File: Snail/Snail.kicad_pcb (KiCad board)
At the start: 2 copper layers, 16 parts, among them J1 Arduino Nano SuperMini, SW0 SW_Push, SW1 SW_Push, SW2 SW_Push, SW3 SW_Push

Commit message: Lay out LED matrix
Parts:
- added C1: 10u, Capacitor_SMD:C_0603_1608Metric, F.Cu at (48.6, 79.7)
- added C105: 100n, Capacitor_SMD:C_0402_1005Metric, F.Cu at (76.0, 60.0)
- added C106: 100n, Capacitor_SMD:C_0402_1005Metric, F.Cu at (63.5, 60.0)
- added C107: 100n, Capacitor_SMD:C_0402_1005Metric, F.Cu at (51.0, 60.0)
- added C108: 100n, Capacitor_SMD:C_0402_1005Metric, F.Cu at (38.5, 60.0)
- added C109: 100n, Capacitor_SMD:C_0402_1005Metric, F.Cu at (26.0, 60.0)
- added C110: 100n, Capacitor_SMD:C_0402_1005Metric, F.Cu at (34.0, 53.0)
- added C111: 100n, Capacitor_SMD:C_0402_1005Metric, F.Cu at (46.5, 53.0)
- added C112: 100n, Capacitor_SMD:C_0402_1005Metric, F.Cu at (59.0, 53.0)
- added C113: 100n, Capacitor_SMD:C_0402_1005Metric, F.Cu at (71.5, 53.0)
- added C114: 100n, Capacitor_SMD:C_0402_1005Metric, F.Cu at (84.0, 53.0)
- added C115: 100n, Capacitor_SMD:C_0402_1005Metric, F.Cu at (76.0, 42.0)
- added C116: 100n, Capacitor_SMD:C_0402_1005Metric, F.Cu at (63.5, 42.0)
- added C117: 100n, Capacitor_SMD:C_0402_1005Metric, F.Cu at (51.0, 42.0)
- added C118: 100n, Capacitor_SMD:C_0402_1005Metric, F.Cu at (38.5, 42.0)
- added C119: 100n, Capacitor_SMD:C_0402_1005Metric, F.Cu at (26.0, 42.0)
- added C120: 100n, Capacitor_SMD:C_0402_1005Metric, F.Cu at (34.0, 35.0)
- added C121: 100n, Capacitor_SMD:C_0402_1005Metric, F.Cu at (46.5, 35.0)
- added C122: 100n, Capacitor_SMD:C_0402_1005Metric, F.Cu at (59.0, 35.0)
- added C123: 100n, Capacitor_SMD:C_0402_1005Metric, F.Cu at (71.5, 35.0)
- added C124: 100n, Capacitor_SMD:C_0402_1005Metric, F.Cu at (84.0, 35.0)
- added C125: 100n, Capacitor_SMD:C_0402_1005Metric, F.Cu at (76.0, 24.0)
- added C126: 100n, Capacitor_SMD:C_0402_1005Metric, F.Cu at (63.5, 24.0)
- added C127: 100n, Capacitor_SMD:C_0402_1005Metric, F.Cu at (51.0, 24.0)
- added C128: 100n, Capacitor_SMD:C_0402_1005Metric, F.Cu at (38.5, 24.0)
- added C129: 100n, Capacitor_SMD:C_0402_1005Metric, F.Cu at (26.0, 24.0)
- added C130: 100n, Capacitor_SMD:C_0402_1005Metric, F.Cu at (34.0, 17.0)
- added C131: 100n, Capacitor_SMD:C_0402_1005Metric, F.Cu at (46.5, 17.0)
- added C132: 100n, Capacitor_SMD:C_0402_1005Metric, F.Cu at (59.0, 17.0)
- added C133: 100n, Capacitor_SMD:C_0402_1005Metric, F.Cu at (71.5, 17.0)
- added C134: 100n, Capacitor_SMD:C_0402_1005Metric, F.Cu at (84.0, 17.0)
- added C2: 10u, Capacitor_SMD:C_0603_1608Metric, F.Cu at (51.1, 79.7)
- added D1: 1N5819, Diode_SMD:D_SOD-323, F.Cu at (55.9, 84.8)
- added D105: WS2812B, Local:LED_ARGB_5050, F.Cu at (80.0, 61.0)
- added D106: WS2812B, Local:LED_ARGB_5050, F.Cu at (67.5, 61.0)
- added D107: WS2812B, Local:LED_ARGB_5050, F.Cu at (55.0, 61.0)
- added D108: WS2812B, Local:LED_ARGB_5050, F.Cu at (42.5, 61.0)
- added D109: WS2812B, Local:LED_ARGB_5050, F.Cu at (30.0, 61.0)
- added D110: WS2812B, Local:LED_ARGB_5050, F.Cu at (30.0, 52.0)
- added D111: WS2812B, Local:LED_ARGB_5050, F.Cu at (42.5, 52.0)
- added D112: WS2812B, Local:LED_ARGB_5050, F.Cu at (55.0, 52.0)
- added D113: WS2812B, Local:LED_ARGB_5050, F.Cu at (67.5, 52.0)
- added D114: WS2812B, Local:LED_ARGB_5050, F.Cu at (80.0, 52.0)
- added D115: WS2812B, Local:LED_ARGB_5050, F.Cu at (80.0, 43.0)
- added D116: WS2812B, Local:LED_ARGB_5050, F.Cu at (67.5, 43.0)
- added D117: WS2812B, Local:LED_ARGB_5050, F.Cu at (55.0, 43.0)
- added D118: WS2812B, Local:LED_ARGB_5050, F.Cu at (42.5, 43.0)
- added D119: WS2812B, Local:LED_ARGB_5050, F.Cu at (30.0, 43.0)
- added D120: WS2812B, Local:LED_ARGB_5050, F.Cu at (30.0, 34.0)
- added D121: WS2812B, Local:LED_ARGB_5050, F.Cu at (42.5, 34.0)
- added D122: WS2812B, Local:LED_ARGB_5050, F.Cu at (55.0, 34.0)
- added D123: WS2812B, Local:LED_ARGB_5050, F.Cu at (67.5, 34.0)
- added D124: WS2812B, Local:LED_ARGB_5050, F.Cu at (80.0, 34.0)
- added D125: WS2812B, Local:LED_ARGB_5050, F.Cu at (80.0, 25.0)
- added D126: WS2812B, Local:LED_ARGB_5050, F.Cu at (67.5, 25.0)
- added D127: WS2812B, Local:LED_ARGB_5050, F.Cu at (55.0, 25.0)
- added D128: WS2812B, Local:LED_ARGB_5050, F.Cu at (42.5, 25.0)
- added D129: WS2812B, Local:LED_ARGB_5050, F.Cu at (30.0, 25.0)
- added D130: WS2812B, Local:LED_ARGB_5050, F.Cu at (30.0, 16.0)
- added D131: WS2812B, Local:LED_ARGB_5050, F.Cu at (42.5, 16.0)
- added D132: WS2812B, Local:LED_ARGB_5050, F.Cu at (55.0, 16.0)
- added D133: WS2812B, Local:LED_ARGB_5050, F.Cu at (67.5, 16.0)
- added D134: WS2812B, Local:LED_ARGB_5050, F.Cu at (80.0, 16.0)
- added Q1: MMBT3904, Package_TO_SOT_SMD:SOT-23, F.Cu at (51.7, 84.3)
- added R1: 4.7k, Resistor_SMD:R_0402_1005Metric, F.Cu at (48.5, 83.3)
- added R2: 10, Resistor_SMD:R_0402_1005Metric, F.Cu at (55.9, 83.2)
- moved BZ1 7.13 mm to (58.2, 95.0), turned to 180 degrees
- moved SW0 4.74 mm to (75.6, 81.2)
- moved SW3 4.74 mm to (66.6, 89.5)
- moved J1 4.74 mm to (35.1, 89.7)
- moved SW1 4.74 mm to (84.0, 89.2)
- moved SW2 4.74 mm to (75.7, 97.9)
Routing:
- net +5V: track 11.6 -> 81.5 mm, vias 6 -> 42
- net Net-(D130-DOUT): track 0.00 -> 17.9 mm
- net Net-(D120-DOUT): track 0.00 -> 17.9 mm
- net Net-(D110-DOUT): track 0.00 -> 17.9 mm
- net Net-(D125-DOUT): track 0.00 -> 17.9 mm
- net Net-(D115-DOUT): track 0.00 -> 17.9 mm
- net Net-(D105-DOUT): track 0.00 -> 17.9 mm
- net Net-(D132-DOUT): track 0.00 -> 8.97 mm
- net Net-(D131-DOUT): track 0.00 -> 8.97 mm
- net Net-(D128-DOUT): track 0.00 -> 8.97 mm
- net Net-(D127-DOUT): track 0.00 -> 8.97 mm
- net Net-(D126-DOUT): track 0.00 -> 8.97 mm
- net Net-(D122-DOUT): track 0.00 -> 8.97 mm
- net Net-(D121-DOUT): track 0.00 -> 8.97 mm
- net Net-(D118-DOUT): track 0.00 -> 8.97 mm
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
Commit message: 🚧 All components layout
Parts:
- added C135: 100n, Capacitor_SMD:C_0402_1005Metric, F.Cu at (120.2, 36.4)
- added C136: 100n, Capacitor_SMD:C_0402_1005Metric, F.Cu at (112.7, 36.4)
- added C137: 100n, Capacitor_SMD:C_0402_1005Metric, F.Cu at (105.2, 36.4)
- added D135: WS2812B, Local:LED_ARGB_3528, F.Cu at (121.0, 38.5)
- added D136: WS2812B, Local:LED_ARGB_3528, F.Cu at (113.5, 38.5)
- added D137: WS2812B, Local:LED_ARGB_3528, F.Cu at (106.0, 38.5)
- moved BZ1 50.6 mm to (98.2, 126.0)
- moved SW1 50.5 mm to (124.0, 120.0)
- moved SW2 50.1 mm to (115.0, 129.0)
- moved D1 50.0 mm to (95.9, 114.8)
- moved R2 50.0 mm to (95.9, 113.2)
- moved C1 50.0 mm to (88.6, 109.7)
- moved C100 50.0 mm to (74.0, 101.0)
- moved C101 50.0 mm to (86.5, 101.0)
- moved C102 50.0 mm to (99.0, 101.0)
- moved C103 50.0 mm to (111.5, 101.0)
- moved C104 50.0 mm to (124.0, 101.0)
- moved C105 50.0 mm to (116.0, 90.0)
- moved C106 50.0 mm to (103.5, 90.0)
- moved C107 50.0 mm to (91.0, 90.0)
- moved C108 50.0 mm to (78.5, 90.0)
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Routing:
- net +5V: track 81.5 -> 102.3 mm
- net /LIGHT_SD: track 0.00 -> 16.9 mm
- net Net-(BZ1--): track 0.00 -> 14.9 mm
- net Net-(BZ1-+): track 0.00 -> 13.6 mm
- net Net-(D134-DOUT): track 0.00 -> 7.80 mm
- net Net-(D136-DOUT): track 0.00 -> 4.56 mm
- net Net-(D135-DOUT): track 0.00 -> 4.56 mm
- net GND: track 0.00 -> 1.86 mm, vias 77 -> 81
- net Net-(Q1-B): track 0.00 -> 1.77 mm

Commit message: Finish layout & routing
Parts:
- moved SW2 2.60 mm to (114.0, 126.6)
- moved SW1 2.44 mm to (122.0, 118.6)
- moved BZ1 1.40 mm to (98.2, 124.6)
- moved C1 1.40 mm to (88.6, 108.3)
- moved C2 1.40 mm to (91.1, 108.3)
- moved J1 1.40 mm to (75.0, 118.3)
- moved R2 1.40 mm to (95.9, 111.8)
- moved SW3 1.40 mm to (106.0, 118.6)
- moved D1 1.40 mm to (95.9, 113.4)
- moved Q1 1.40 mm to (91.7, 112.9)
- moved R1 1.40 mm to (88.5, 111.9)
- moved C130 1.10 mm to (74.0, 48.1)
- moved C131 1.10 mm to (86.5, 48.1)
- moved C132 1.10 mm to (99.0, 48.1)
- moved C133 1.10 mm to (111.5, 48.1)
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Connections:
- J1 pad 10: unconnected-(J1-Pin_10-Pad10) -> /KEY_0
- J1 pad 11: unconnected-(J1-Pin_11-Pad11) -> /KEY_3
- J1 pad 12: /KEY_0 -> unconnected-(J1-Pin_12-Pad12)
- J1 pad 13: /KEY_1 -> unconnected-(J1-Pin_13-Pad13)
- J1 pad 14: /KEY_2 -> unconnected-(J1-Pin_14-Pad14)
- J1 pad 15: /KEY_3 -> /BUZZER
- J1 pad 6: /BUZZER -> unconnected-(J1-Pin_6-Pad6)
- J1 pad 8: unconnected-(J1-Pin_8-Pad8) -> /KEY_1
- J1 pad 9: unconnected-(J1-Pin_9-Pad9) -> /KEY_2
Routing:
- net +5V: track 102.3 -> 490.7 mm, vias 42 -> 0
- net /KEY_1: track 0.00 -> 69.3 mm
- net /KEY_2: track 0.00 -> 45.8 mm
- net /KEY_0: track 0.00 -> 41.5 mm
- net /KEY_3: track 0.00 -> 26.3 mm
- net Net-(D129-DOUT): track 0.00 -> 11.4 mm
- net Net-(D119-DOUT): track 0.00 -> 11.4 mm
- net Net-(D109-DOUT): track 0.00 -> 11.4 mm
- net Net-(D114-DOUT): track 0.00 -> 9.62 mm
- net Net-(D104-DOUT): track 0.00 -> 9.62 mm
- net Net-(D124-DOUT): track 0.00 -> 9.62 mm
- net Net-(D115-DOUT): track 17.9 -> 8.97 mm
- net Net-(D110-DOUT): track 17.9 -> 8.97 mm
- net Net-(D105-DOUT): track 17.9 -> 8.97 mm
- net Net-(D100-DOUT): track 17.9 -> 8.97 mm
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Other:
- board outline added: 64 x 98 mm

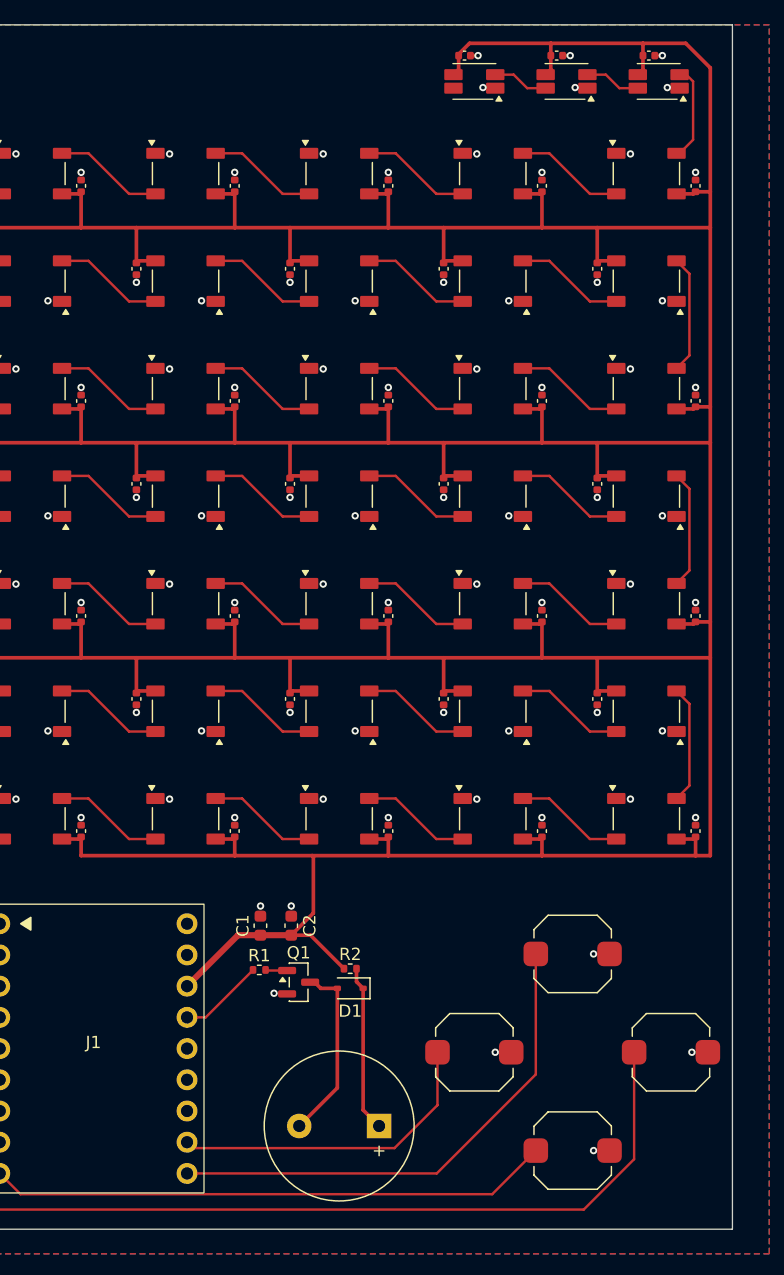
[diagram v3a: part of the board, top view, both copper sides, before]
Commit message: Revise board design for rounded tracks & teardrops
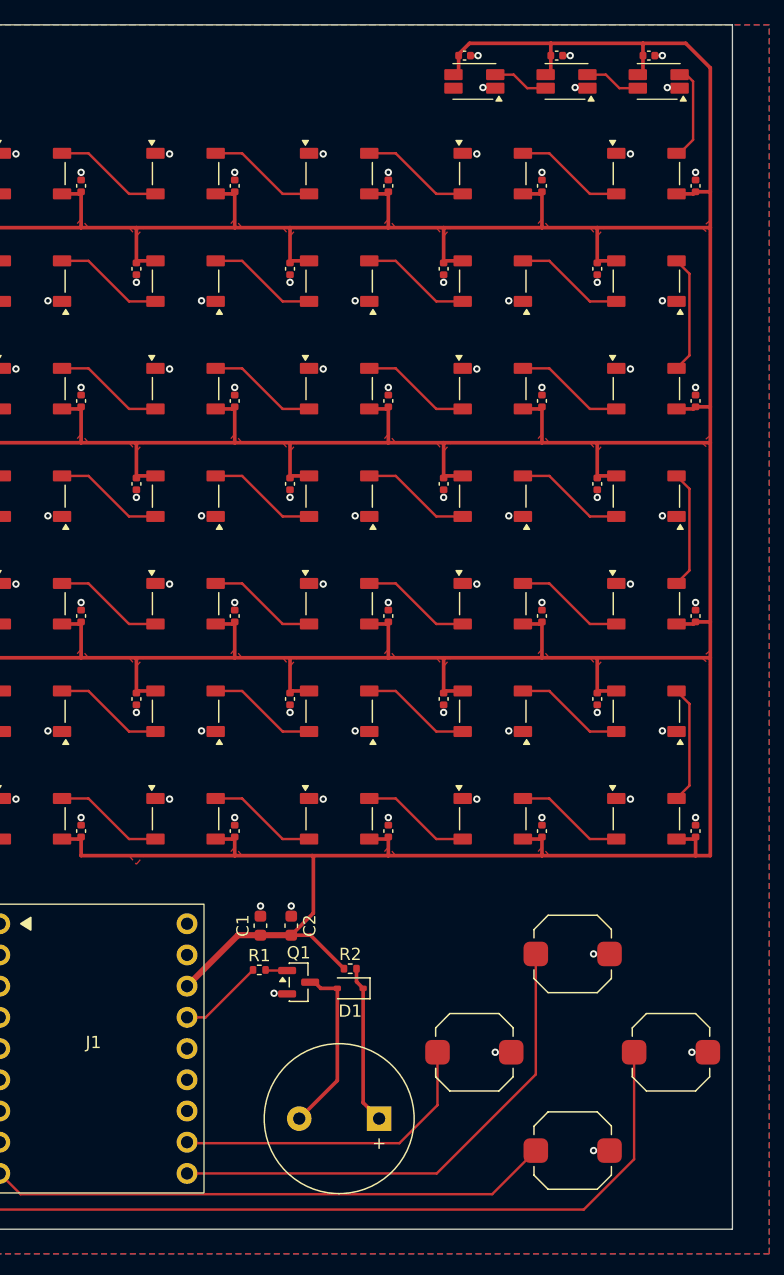
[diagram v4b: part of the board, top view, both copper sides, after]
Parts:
- moved BZ1 0.60 mm to (98.2, 124.0)
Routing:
- net +5V: track 490.7 -> 491.5 mm
- net Net-(BZ1--): track 14.9 -> 14.3 mm
- net Net-(BZ1-+): track 13.6 -> 13.0 mm
- added copper zone on F.Cu, net +5V

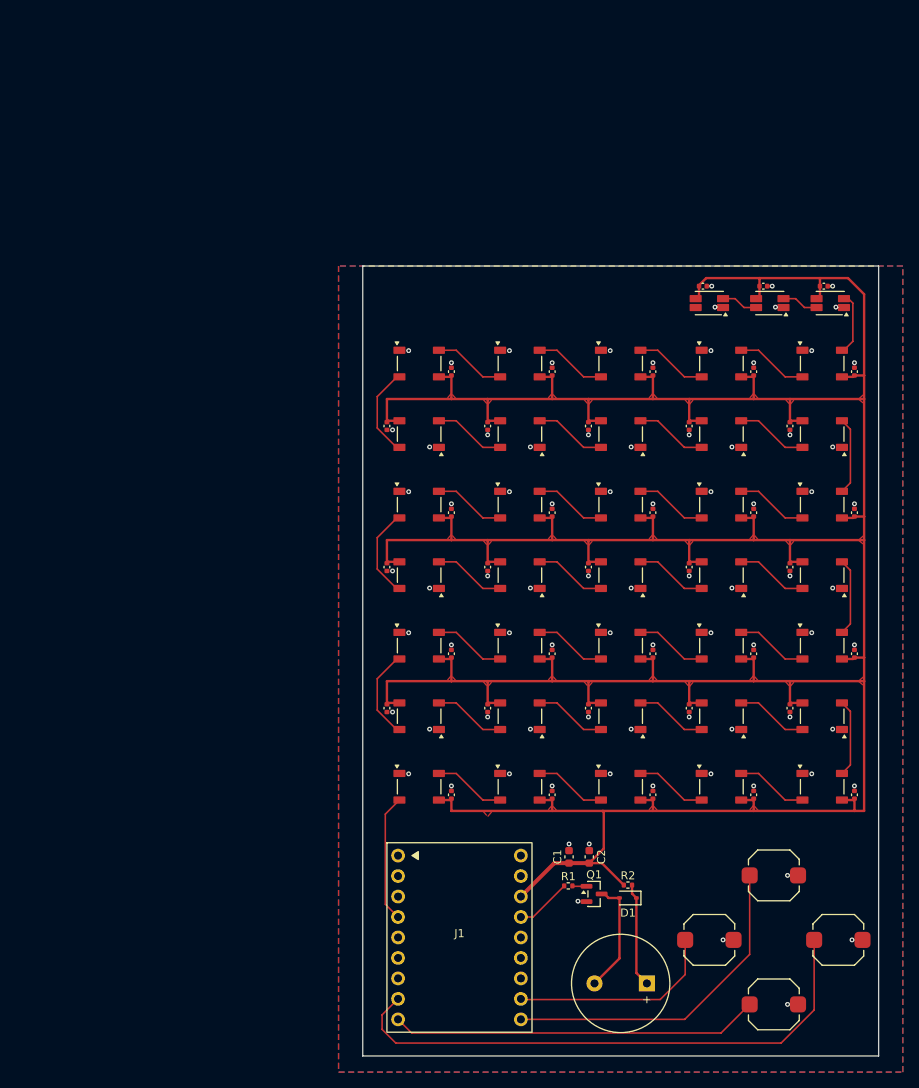
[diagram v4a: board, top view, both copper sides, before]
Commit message: Add stitching vias
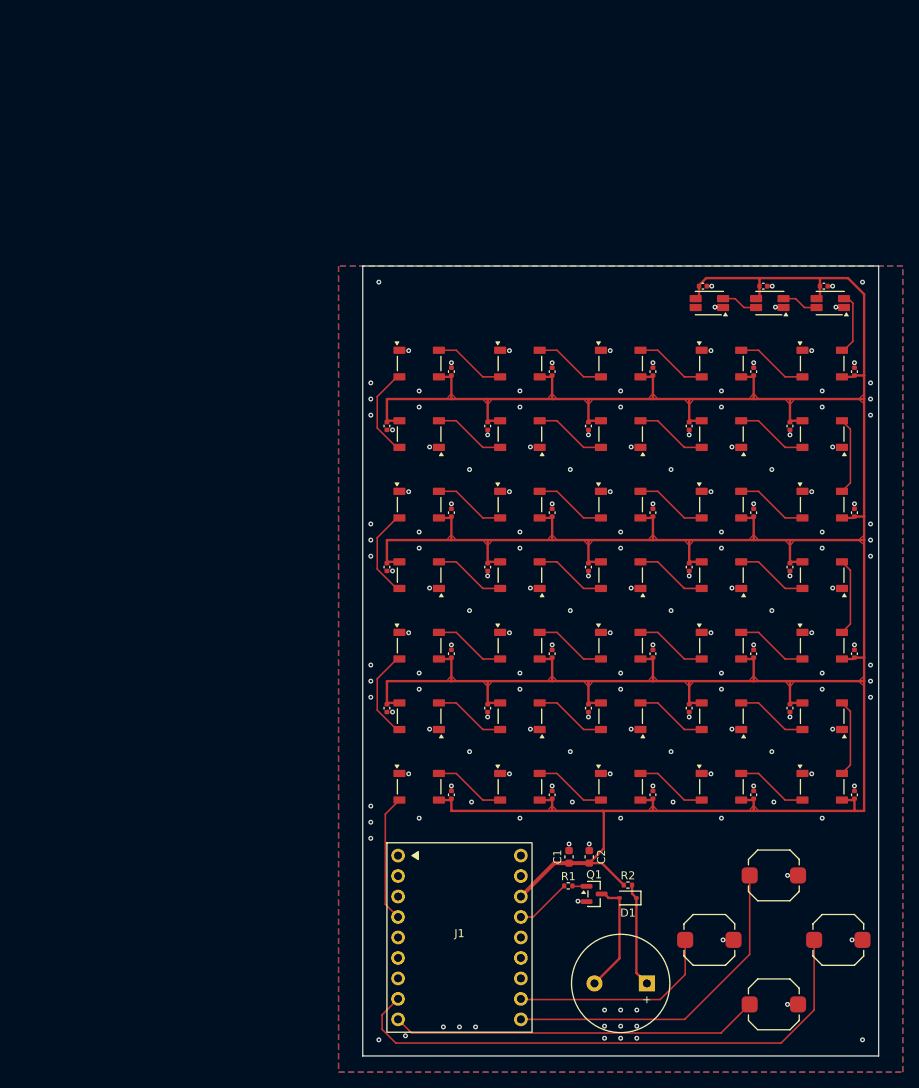
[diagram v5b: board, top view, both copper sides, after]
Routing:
- net GND: vias 83 -> 172

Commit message: Finalize by silkscreen
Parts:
- added G***: LOGO, LOGO, B.Cu at (118.4, 129.9)
- added G***: LOGO, LOGO, B.Cu at (123.5, 129.7)
- moved D1 0.20 mm to (95.7, 113.4)
- moved R2 0.20 mm to (95.7, 111.8)
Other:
- board text added: "<26-"
- board text added: ">"
- board text added: "Rev. 1"
- board text added: "雨水"

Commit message: hw: Update files with actual mounted component value
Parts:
- R2: value 10 -> 220
